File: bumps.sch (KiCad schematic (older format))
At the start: 134 parts, among them M1 CONN_1, M2 CONN_1, M3 CONN_1, P1 DIL6, P10 Mot-A, P11 Mot-A, P12 Mot-X, P13 T1, P14 T2, P15 T3, P16 MPower, P17 PWM-2, P18 PWM-1, P19 END-X, P2 DIL6, P20 END-Y, P21 END-Z, P22 Mot-X, P23 Mot-Y, P24 Mot-Y, P25 Mot-Z, P26 Mot-Z, P27 Aux, P28 KillSwitch, P29 PWM, P3 Mot-E, P4 Mot-E, P5 DIL6, P6 DIL6, P7 DIL6, P8 P8 Header, P9 P9 Header, Q1 IRLB8743PBF, Q2 IRLB8743PBF, Q3 FDS9926A, Q4 FDS9926A, U1 Motor-2, U2 Motor-4, U3 Motor-5, U4 Motor-3, U5 Motor-1, U6 MC34063, U7 AP1117/3.3, U8 Opto

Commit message: o Adding fuse holder (footprint and schematic). o .. work in progress. Attempt to make things fit.
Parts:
- removed F1: FUSE, Fuse_Holders_and_Fuses:Fuse_TE5_Littlefuse-395Series, symbol FUSE
- added P30, P31: CONN_01X01, bumps:FuseBlade, symbol CONN_01X01
- R2, R3: footprint SMD_Packages:SM0805 -> Resistors_SMD:R_0805
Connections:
- net labels added: Power-IN
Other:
- moved on the sheet: M1, M2, M3
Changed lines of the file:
@@
-	1    0    0    -1
-$EndComp
-$Comp
-L FUSE F1
-U 1 1 52EE1508
-P 1550 9050
-F 0 "F1" H 1650 9100 40  0000 C CNN
-F 1 "FUSE" H 1450 9000 40  0000 C CNN
-F 2 "Fuse_Holders_and_Fuses:Fuse_TE5_Littlefuse-395Series" H 1550 9050 60  0001 C CNN
-F 3 "" H 1550 9050 60  0000 C CNN
-	1    1550 9050
 	1    0    0    -1
 $EndComp
@@
 L PWR_FLAG #FLG036
 U 1 1 53019B49
-P 1850 9000
-F 0 "#FLG036" H 1850 9095 30  0001 C CNN
-F 1 "PWR_FLAG" H 1850 9180 30  0000 C CNN
-F 2 "" H 1850 9000 60  0001 C CNN
-F 3 "" H 1850 9000 60  0000 C CNN
-	1    1850 9000
-	1    0    0    -1
+P 1850 9100
+F 0 "#FLG036" H 1850 9195 30  0001 C CNN
+F 1 "PWR_FLAG" H 1850 9280 30  0000 C CNN
+F 2 "" H 1850 9100 60  0001 C CNN
+F 3 "" H 1850 9100 60  0000 C CNN
+	1    1850 9100
+	-1   0    0    1
 $EndComp
 $Comp
@@
 L CONN_01X01 M1
 U 1 1 53137A56
-P 1800 9450
-F 0 "M1" H 1880 9450 40  0000 L CNN
-F 1 "CONN_1" H 1800 9505 30  0001 C CNN
-F 2 "Connect:1pin" H 1800 9450 60  0001 C CNN
-F 3 "" H 1800 9450 60  0000 C CNN
-	1    1800 9450
+P 2750 9500
+F 0 "M1" H 2830 9500 40  0000 L CNN
+F 1 "CONN_1" H 2750 9555 30  0001 C CNN
+F 2 "Connect:1pin" H 2750 9500 60  0001 C CNN
+F 3 "" H 2750 9500 60  0000 C CNN
+	1    2750 9500
 	0    -1   -1   0
 $EndComp
@@
 L CONN_01X01 M2
 U 1 1 53137A6A
-P 2000 9450
-F 0 "M2" H 2080 9450 40  0000 L CNN
-F 1 "CONN_1" H 2000 9505 30  0001 C CNN
-F 2 "Connect:1pin" H 2000 9450 60  0001 C CNN
-F 3 "" H 2000 9450 60  0000 C CNN
-	1    2000 9450
+P 2950 9500
+F 0 "M2" H 3030 9500 40  0000 L CNN
+F 1 "CONN_1" H 2950 9555 30  0001 C CNN
+F 2 "Connect:1pin" H 2950 9500 60  0001 C CNN
+F 3 "" H 2950 9500 60  0000 C CNN
+	1    2950 9500
 	0    -1   -1   0
 $EndComp
@@
 L CONN_01X01 M3
 U 1 1 5313908A
-P 2200 9450
-F 0 "M3" H 2280 9450 40  0000 L CNN
-F 1 "CONN_1" H 2200 9505 30  0001 C CNN
-F 2 "Connect:1pin" H 2200 9450 60  0001 C CNN
-F 3 "" H 2200 9450 60  0000 C CNN
-	1    2200 9450
+P 3150 9500
+F 0 "M3" H 3230 9500 40  0000 L CNN
+F 1 "CONN_1" H 3150 9555 30  0001 C CNN
+F 2 "Connect:1pin" H 3150 9500 60  0001 C CNN
+F 3 "" H 3150 9500 60  0000 C CNN
+	1    3150 9500
 	0    -1   -1   0
 $EndComp
@@
 F 0 "R3" V 10500 8150 40  0000 C CNN
 F 1 "4k7" V 10607 8151 40  0000 C CNN
-F 2 "SMD_Packages:SM0805" V 10530 8150 30  0001 C CNN
+F 2 "Resistors_SMD:R_0805" V 10530 8150 30  0001 C CNN
 F 3 "" H 10600 8150 30  0000 C CNN
 	1    10600 8150
@@
 F 0 "R2" V 8550 7850 40  0000 C CNN
 F 1 "330" V 8657 7851 40  0000 C CNN
-F 2 "SMD_Packages:SM0805" V 8580 7850 30  0001 C CNN
+F 2 "Resistors_SMD:R_0805" V 8580 7850 30  0001 C CNN
 F 3 "" H 8650 7850 30  0000 C CNN
 	1    8650 7850
@@
 	1150 9050 1300 9050
 Wire Wire Line
-	1800 9050 2000 9050
+	1650 9050 2000 9050
 Wire Wire Line
 	4300 8500 4650 8500
@@
 Connection ~ 3450 7950
 Connection ~ 3450 7700
-Wire Wire Line
-	1850 9000 1850 9050
 Connection ~ 1850 9050
 Wire Wire Line
@@
 	-1   0    0    1
 $EndComp
+$Comp
+L CONN_01X01 P30
+U 1 1 5570EE85
+P 1300 8850
+F 0 "P30" H 1300 8950 50  0000 C CNN
+F 1 "CONN_01X01" V 1400 8850 50  0000 C CNN
+F 2 "bumps:FuseBlade" H 1300 8850 60  0001 C CNN
+F 3 "" H 1300 8850 60  0000 C CNN
+	1    1300 8850
+	0    -1   -1   0
+$EndComp
+Wire Wire Line
+	1850 9050 1850 9100
+$Comp
+L CONN_01X01 P31
+U 1 1 5570F5CA
+P 1650 8850
+F 0 "P31" H 1650 8950 50  0000 C CNN
+F 1 "CONN_01X01" V 1750 8850 50  0000 C CNN
+F 2 "bumps:FuseBlade" H 1650 8850 60  0001 C CNN
+F 3 "" H 1650 8850 60  0000 C CNN
+	1    1650 8850
+	0    -1   -1   0
+$EndComp
+Text Label 850  9000 0    60   ~ 0
+Power-IN
 $EndSCHEMATC

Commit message: o intermediate state.
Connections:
- wire segments 260 -> 255
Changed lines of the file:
@@
 	5800 4650 5800 4700
 Wire Wire Line
-	4300 4350 4300 4450
-Wire Wire Line
 	3900 4050 4300 4050
 Wire Wire Line
@@
 Wire Wire Line
 	9950 5050 9950 5100
-Wire Wire Line
-	8450 4750 8450 4850
 Wire Wire Line
 	7250 4250 7250 4650
@@
 	9950 1750 9950 1800
 Wire Wire Line
-	8450 1450 8450 1550
-Wire Wire Line
 	7250 950  7250 1350
 Connection ~ 7250 1150
@@
 	9950 3400 9950 3450
 Wire Wire Line
-	8450 3100 8450 3200
-Wire Wire Line
 	7250 2600 7250 3000
 Connection ~ 7250 2800
@@
 Wire Wire Line
 	5800 6400 5800 6450
-Wire Wire Line
-	4300 6100 4300 6200
 Wire Wire Line
 	3100 5600 3100 6000
@@
 Text Label 850  9000 0    60   ~ 0
 Power-IN
+Text GLabel 4300 4350 0    60   Input ~ 0
+~EStop
+Text GLabel 4300 6100 0    60   Input ~ 0
+~EStop
+Text GLabel 8450 4750 0    60   Input ~ 0
+~EStop
+Text GLabel 8450 3100 0    60   Input ~ 0
+~EStop
+Text GLabel 8450 1450 0    60   Input ~ 0
+~EStop
 $EndSCHEMATC

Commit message: o Bring to latest state of kicad library. o Now checking in also bumps-cache: learned that it   is effectively the 'project library' keeping track of   the symbols being used. o (was done in a branch, squashed together now).
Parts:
- C1, C12, C2, C3, C4, C5, C7, C8: symbol CAPAPOL -> CP
- D1: symbol DIODESCH -> D_Schottky
- D10, D11: footprint Diodes_ThroughHole:Diode_DO-41_SOD81_Vertical_KathodeUp -> Diodes_ThroughHole:Diode_DO-41_SOD81_Vertical_AnodeUp; symbol DIODE -> D_Schottky
- D12, D13, D14, D15, D16, D17, D18, D19, D20, D21: symbol LED -> Led_Small
- Q1, Q2: footprint Transistors_TO-220:TO-220_FET-GDS_Vertical_LargePads -> Transistors_TO-220:TO-220_Neutral123_Vertical_LargePads; symbol MOSFET_N -> Q_NMOS_GDS
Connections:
- wire segments 255 -> 252
- no-connect marks 47 -> 52
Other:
- moved on the sheet: C13, C14, C15, C16, C17, C20, C21, C22, C23, C24, C6, D2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

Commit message: o use standard opto PC817 footprint.
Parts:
- U8: value Opto -> PC817; symbol OPTO-TRANSISTOR4 -> PC817
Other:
- moved on the sheet: P28, R2, R3
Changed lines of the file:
@@
 VDD_3V3
 $Comp
-L OPTO-TRANSISTOR4 U8
+L PC817 U8
 U 1 1 556F9659
-P 9550 8000
-F 0 "U8" H 9750 8250 60  0000 C CNN
-F 1 "Opto" H 9550 7750 60  0000 C CNN
-F 2 "bumps:DIL-4" H 9550 8000 60  0001 C CNN
-F 3 "" H 9550 8000 60  0000 C CNN
-	1    9550 8000
+P 8350 7900
+F 0 "U8" H 8200 7650 60  0000 C CNN
+F 1 "PC817" H 8450 7650 60  0000 C CNN
+F 2 "bumps:DIL-4" H 8350 7900 60  0001 C CNN
+F 3 "" H 8350 7900 60  0000 C CNN
+	1    8350 7900
 	1    0    0    -1
 $EndComp
@@
 L R R3
 U 1 1 556FE6AB
-P 10500 8150
-F 0 "R3" V 10600 8150 40  0000 C CNN
-F 1 "4k7" V 10507 8151 40  0000 C CNN
-F 2 "Resistors_SMD:R_0805" V 10430 8150 30  0001 C CNN
-F 3 "" H 10500 8150 30  0000 C CNN
-	1    10500 8150
+P 8800 8000
+F 0 "R3" V 8900 8000 40  0000 C CNN
+F 1 "4k7" V 8807 8001 40  0000 C CNN
+F 2 "Resistors_SMD:R_0805" V 8730 8000 30  0001 C CNN
+F 3 "" H 8800 8000 30  0000 C CNN
+	1    8800 8000
 	0    -1   1    0
 $EndComp
-Text GLabel 10150 7850 2    50   Input ~ 0
+Text GLabel 8650 7800 2    50   Input ~ 0
 VDD_3V3
-Text GLabel 10250 8000 2    60   Output ~ 0
+Text GLabel 9050 7900 2    60   Output ~ 0
 ~EStop
 $Comp
 L GND #PWR051
 U 1 1 55714D22
-P 10650 8200
-F 0 "#PWR051" H 10650 8200 30  0001 C CNN
-F 1 "GND" H 10650 8130 30  0001 C CNN
-F 2 "" H 10650 8200 60  0001 C CNN
-F 3 "" H 10650 8200 60  0000 C CNN
-	1    10650 8200
+P 8950 8050
+F 0 "#PWR051" H 8950 8050 30  0001 C CNN
+F 1 "GND" H 8950 7980 30  0001 C CNN
+F 2 "" H 8950 8050 60  0001 C CNN
+F 3 "" H 8950 8050 60  0000 C CNN
+	1    8950 8050
 	-1   0    0    -1
 $EndComp
-Text Notes 8800 7750 0    60   ~ 0
+Text Notes 7550 7700 0    60   ~ 0
 Normal case: LED on, ~EStop~ pulled to High.
 $Comp
 L R R2
 U 1 1 557180A7
-P 8750 7850
-F 0 "R2" V 8650 7850 40  0000 C CNN
-F 1 "330" V 8757 7851 40  0000 C CNN
-F 2 "Resistors_SMD:R_0805" V 8680 7850 30  0001 C CNN
-F 3 "" H 8750 7850 30  0000 C CNN
-	1    8750 7850
+P 7900 7800
+F 0 "R2" V 7800 7800 40  0000 C CNN
+F 1 "330" V 7907 7801 40  0000 C CNN
+F 2 "Resistors_SMD:R_0805" V 7830 7800 30  0001 C CNN
+F 3 "" H 7900 7800 30  0000 C CNN
+	1    7900 7800
 	0    -1   1    0
 $EndComp
-Text GLabel 8600 7850 0    50   Input ~ 0
+Text GLabel 7750 7800 0    50   Input ~ 0
 VDD_5V
 $Comp
 L GND #PWR052
 U 1 1 5571A73C
-P 8500 8250
-F 0 "#PWR052" H 8500 8250 30  0001 C CNN
-F 1 "GND" H 8500 8180 30  0001 C CNN
-F 2 "" H 8500 8250 60  0001 C CNN
-F 3 "" H 8500 8250 60  0001 C CNN
-	1    8500 8250
+P 7650 8150
+F 0 "#PWR052" H 7650 8150 30  0001 C CNN
+F 1 "GND" H 7650 8080 30  0001 C CNN
+F 2 "" H 7650 8150 60  0001 C CNN
+F 3 "" H 7650 8150 60  0001 C CNN
+	1    7650 8150
 	1    0    0    -1
 $EndComp
-Text Notes 7850 8000 0    60   ~ 0
+Text Notes 7300 8250 1    60   ~ 0
 Switch NC
 Wire Wire Line
@@
 Connection ~ 4500 1250
 Wire Wire Line
-	10150 8150 10350 8150
-Wire Wire Line
-	10250 8000 10200 8000
-Wire Wire Line
-	10200 8000 10200 8150
-Connection ~ 10200 8150
-Wire Wire Line
-	10650 8150 10650 8200
-Wire Wire Line
-	8500 8100 8900 8100
-Wire Wire Line
-	8900 8100 8900 8150
-Wire Wire Line
-	8500 8200 8500 8200
-Wire Wire Line
-	8500 8200 8500 8250
+	8950 8000 8950 8050
+Wire Wire Line
+	7650 8000 8050 8000
+Wire Wire Line
+	7650 8100 7650 8100
+Wire Wire Line
+	7650 8100 7650 8150
 $Comp
 L CONN_01X02 P28
 U 1 1 557008FF
-P 8300 8150
-F 0 "P28" H 8300 8300 50  0000 C CNN
-F 1 "KillSwitch" V 8400 8150 50  0000 C CNN
-F 2 "bumps:WideHeader" H 8300 8150 60  0001 C CNN
-F 3 "" H 8300 8150 60  0000 C CNN
-	1    8300 8150
+P 7450 8050
+F 0 "P28" H 7450 8200 50  0000 C CNN
+F 1 "KillSwitch" V 7550 8050 50  0000 C CNN
+F 2 "bumps:WideHeader" H 7450 8050 60  0001 C CNN
+F 3 "" H 7450 8050 60  0000 C CNN
+	1    7450 8050
 	-1   0    0    1
 $EndComp
@@
 Wire Wire Line
 	2000 7150 2050 7150
+Wire Wire Line
+	8650 8000 8650 7900
+Wire Wire Line
+	8650 7900 9050 7900
 $EndSCHEMATC

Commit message: o Use some current standard components.
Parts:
- C13, C15, C16, C17, C20, C21, C22, C23, C24, C6: footprint SMD_Packages:SM0805 -> Capacitors_SMD:C_0805
- Q3, Q4, U6: footprint SOIC_Packages:SOIC-8_N -> Housings_SOIC:SOIC-8_3.9x4.9mm_Pitch1.27mm
- R10, R11, R12, R13, R14, R15, R16, R17, R18, R19, R20, R21, R22, R23, R24, R25, R26, R27, R28, R29, R30, R31, R32, R33, R34, R35, R36, R37, R38, R39, R40, R41, R42, R43, R6, R7, R8, R9: footprint SMD_Packages:SM0805 -> Resistors_SMD:R_0805
- U8: footprint bumps:DIL-4 -> Housings_DIP:DIP-4_W7.62mm

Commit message: o More standard footprint conversions.
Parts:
- D5, D6, D7: footprint SMD_Packages:SOT23 -> Housings_SOT-23_SOT-143_TSOT-6:SOT-23
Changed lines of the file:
@@
 F 0 "D7" V 10700 6200 60  0000 L CNN
 F 1 "BAT54S" V 10700 5800 60  0000 L CNN
-F 2 "SMD_Packages:SOT23" H 10600 6050 60  0001 C CNN
+F 2 "Housings_SOT-23_SOT-143_TSOT-6:SOT-23" H 10600 6050 60  0001 C CNN
 F 3 "" H 10600 6050 60  0000 C CNN
 	1    10600 6050
@@
 F 0 "D6" V 9500 6150 60  0000 L CNN
 F 1 "BAT54S" V 9500 5800 60  0000 L CNN
-F 2 "SMD_Packages:SOT23" H 9400 6050 60  0001 C CNN
+F 2 "Housings_SOT-23_SOT-143_TSOT-6:SOT-23" H 9400 6050 60  0001 C CNN
 F 3 "" H 9400 6050 60  0000 C CNN
 	1    9400 6050
@@
 F 0 "D5" V 8300 6200 60  0000 L CNN
 F 1 "BAT54S" V 8300 5800 60  0000 L CNN
-F 2 "SMD_Packages:SOT23" H 8200 6050 60  0001 C CNN
+F 2 "Housings_SOT-23_SOT-143_TSOT-6:SOT-23" H 8200 6050 60  0001 C CNN
 F 3 "" H 8200 6050 60  0000 C CNN
 	1    8200 6050

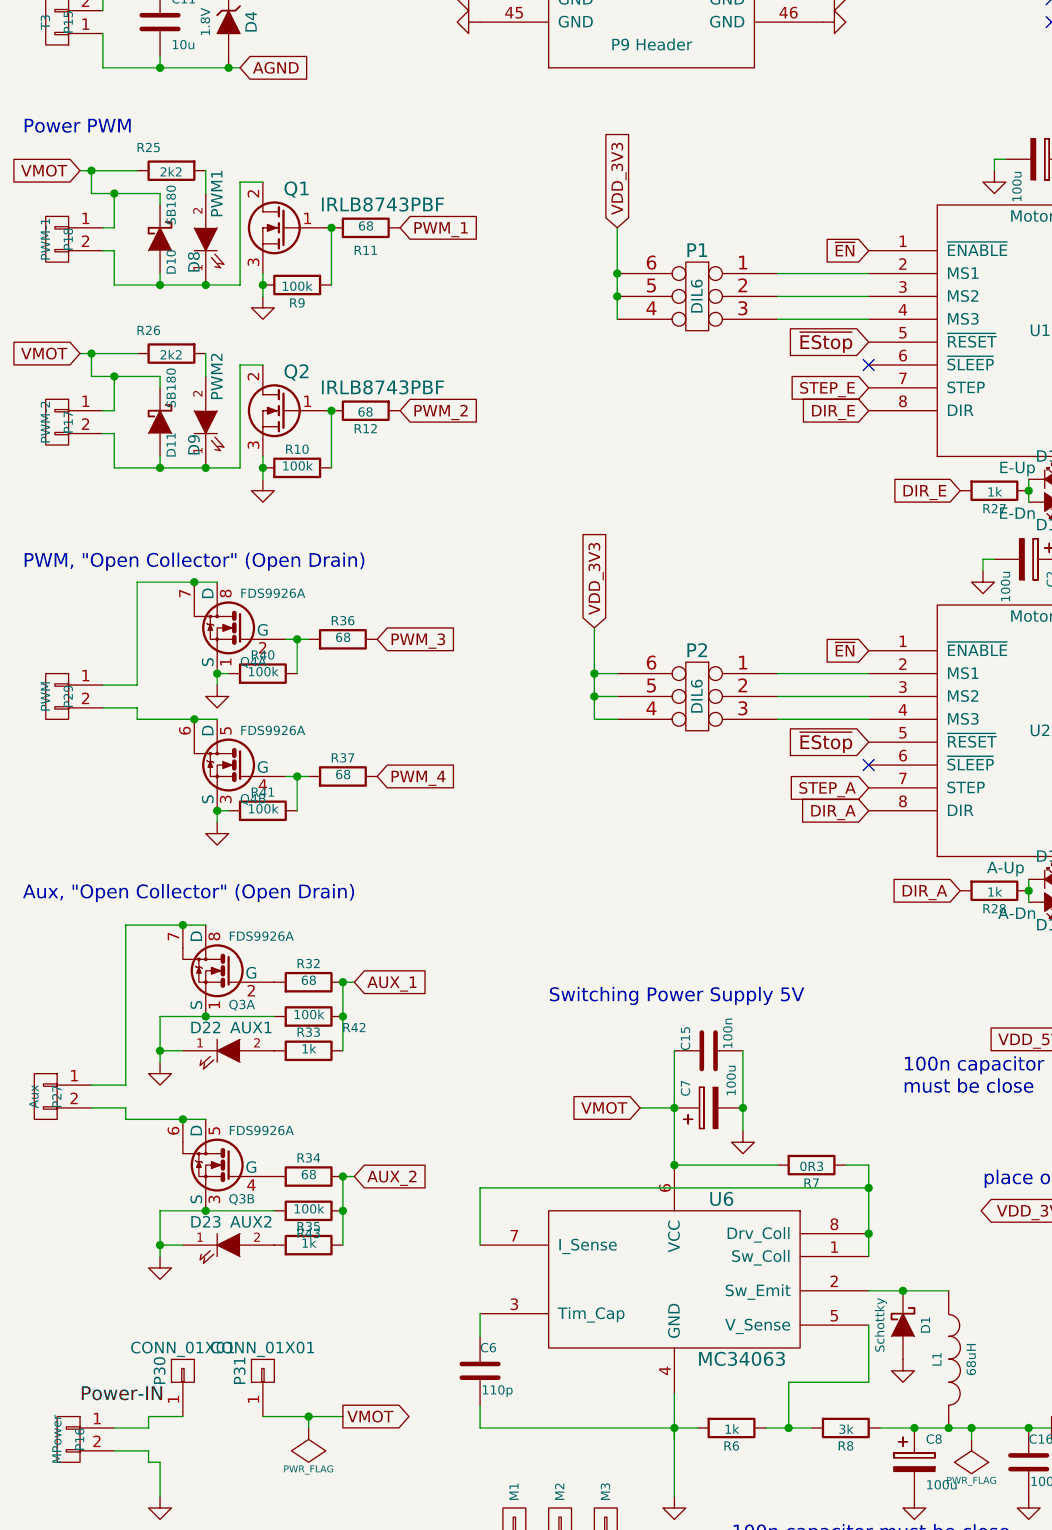
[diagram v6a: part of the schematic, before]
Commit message: o Design for Manufacturing: choose the same kind of diode for the   switching power supply and the snubber diode to reduce different   component BOM count.
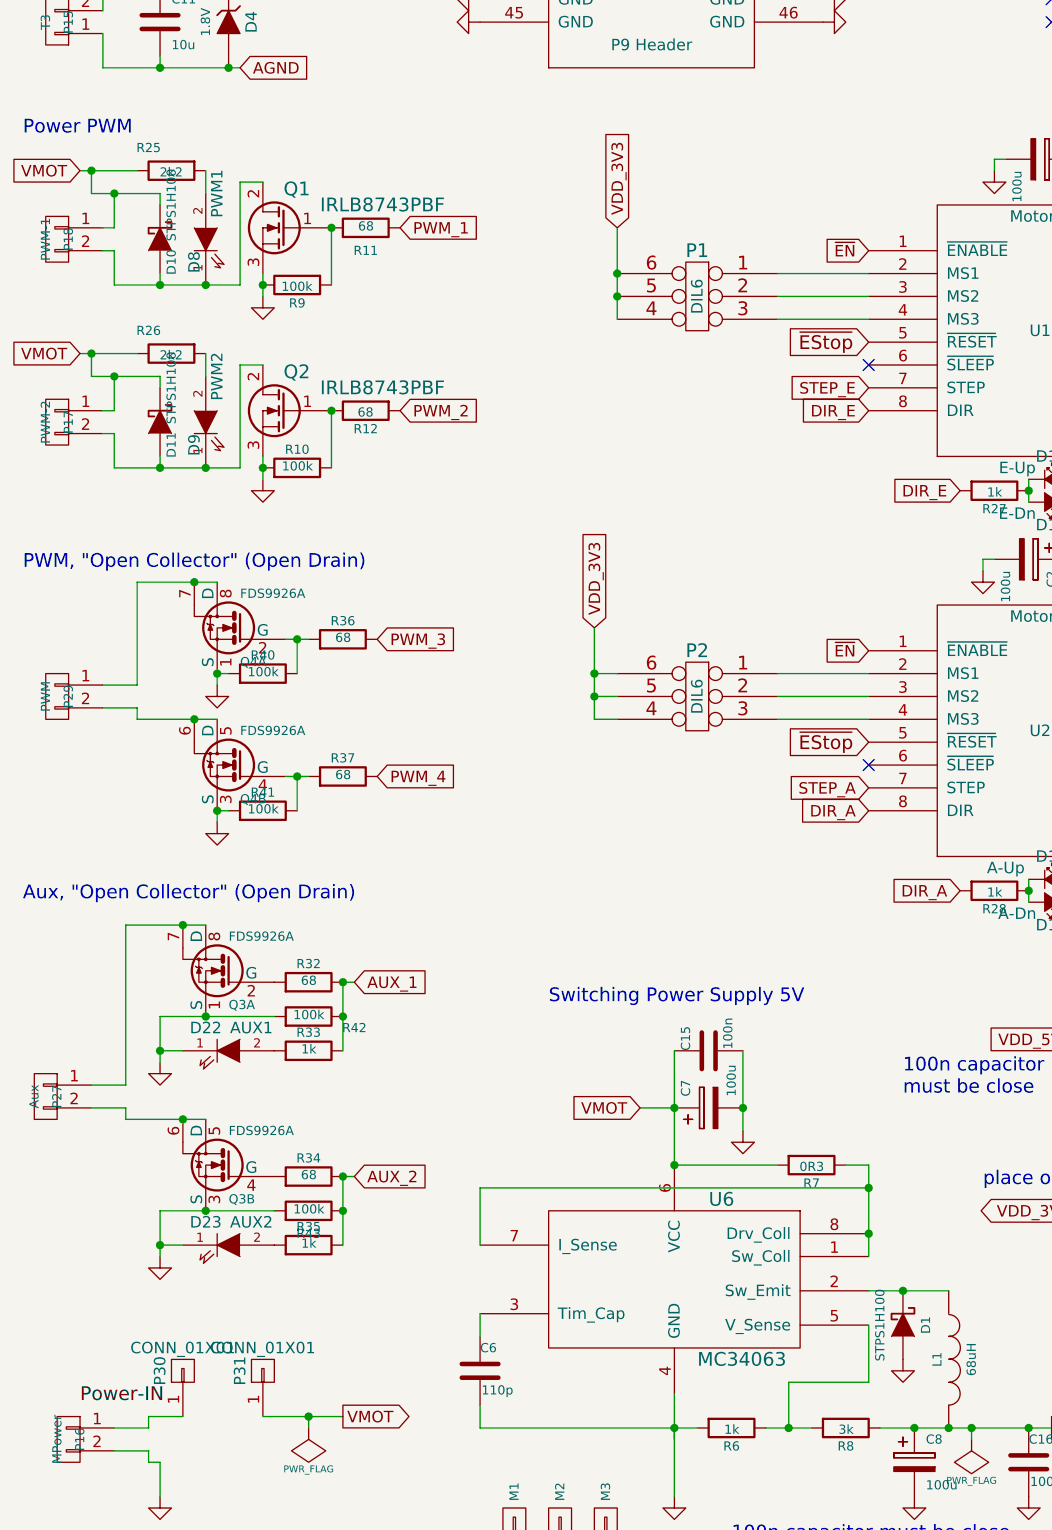
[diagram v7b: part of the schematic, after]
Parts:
- D1: value Schottky -> STPS1H100; footprint Diodes_SMD:Diode-MiniMELF_Standard -> Diodes_SMD:Diode-SMB_Standard
- D10, D11: value SB180 -> STPS1H100; footprint Diodes_ThroughHole:Diode_DO-41_SOD81_Vertical_AnodeUp -> Diodes_SMD:Diode-SMB_Standard
- D2, D3, D4: footprint Diodes_SMD:Diode-MiniMELF_Standard -> Diodes_SMD:SOD-123
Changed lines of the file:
@@
 P 4450 8650
 F 0 "D1" H 4450 8750 40  0000 C CNN
-F 1 "Schottky" H 4450 8550 40  0000 C CNN
-F 2 "Diodes_SMD:Diode-MiniMELF_Standard" H 4450 8650 60  0001 C CNN
-F 3 "" H 4450 8650 60  0000 C CNN
+F 1 "STPS1H100" H 4450 8550 40  0000 C CNN
+F 2 "Diodes_SMD:Diode-SMB_Standard" H 4450 8650 60  0001 C CNN
+F 3 "http://www.st.com/web/en/resource/technical/document/datasheet/CD00001304.pdf" H 4450 8650 60  0001 C CNN
 	1    4450 8650
 	0    1    1    0
@@
 F 0 "D3" H 1500 2150 50  0000 C CNN
 F 1 "1.8V" H 1500 1950 40  0000 C CNN
-F 2 "Diodes_SMD:Diode-MiniMELF_Standard" H 1500 2050 60  0001 C CNN
+F 2 "Diodes_SMD:SOD-123" H 1500 2050 60  0001 C CNN
 F 3 "" H 1500 2050 60  0000 C CNN
 	1    1500 2050
@@
 F 0 "D2" H 1500 1250 50  0000 C CNN
 F 1 "1.8V" H 1500 1050 40  0000 C CNN
-F 2 "Diodes_SMD:Diode-MiniMELF_Standard" H 1500 1150 60  0001 C CNN
+F 2 "Diodes_SMD:SOD-123" H 1500 1150 60  0001 C CNN
 F 3 "" H 1500 1150 60  0000 C CNN
 	1    1500 1150
@@
 F 0 "D4" H 1500 3050 50  0000 C CNN
 F 1 "1.8V" H 1500 2850 40  0000 C CNN
-F 2 "Diodes_SMD:Diode-MiniMELF_Standard" H 1500 2950 60  0001 C CNN
+F 2 "Diodes_SMD:SOD-123" H 1500 2950 60  0001 C CNN
 F 3 "" H 1500 2950 60  0000 C CNN
 	1    1500 2950
@@
 P 1200 3900
 F 0 "D10" H 1300 3950 40  0000 C CNN
-F 1 "SB180" H 1050 3950 40  0000 C CNN
-F 2 "Diodes_ThroughHole:Diode_DO-41_SOD81_Vertical_AnodeUp" H 1200 3900 60  0001 C CNN
+F 1 "STPS1H100" H 1050 3950 40  0000 C CNN
+F 2 "Diodes_SMD:Diode-SMB_Standard" H 1200 3900 60  0001 C CNN
 F 3 "" H 1200 3900 60  0000 C CNN
 	1    1200 3900
@@
 P 1200 4700
 F 0 "D11" H 1300 4750 40  0000 C CNN
-F 1 "SB180" H 1050 4750 40  0000 C CNN
-F 2 "Diodes_ThroughHole:Diode_DO-41_SOD81_Vertical_AnodeUp" H 1200 4700 60  0001 C CNN
+F 1 "STPS1H100" H 1050 4750 40  0000 C CNN
+F 2 "Diodes_SMD:Diode-SMB_Standard" H 1200 4700 60  0001 C CNN
 F 3 "" H 1200 4700 60  0000 C CNN
 	1    1200 4700
@@
 F 1 "CONN_01X01" V 1400 8850 50  0000 C CNN
 F 2 "bumps:FuseBlade" H 1300 8850 60  0001 C CNN
-F 3 "" H 1300 8850 60  0000 C CNN
+F 3 "http://www.keyelco.com/userAssets/file/M60-2p41.pdf" H 1300 8850 60  0001 C CNN
 	1    1300 8850
 	0    -1   -1   0
@@
 F 1 "CONN_01X01" V 1750 8850 50  0000 C CNN
 F 2 "bumps:FuseBlade" H 1650 8850 60  0001 C CNN
-F 3 "" H 1650 8850 60  0000 C CNN
+F 3 "http://www.keyelco.com/userAssets/file/M60-2p41.pdf" H 1650 8850 60  0001 C CNN
 	1    1650 8850
 	0    -1   -1   0

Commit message: o Use BUK9Y43 as power PWM transistor. SMD is easier to solder.
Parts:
- removed D10, D11: STPS1H100, Diodes_SMD:Diode-SMB_Standard, symbol D_Schottky
- removed Q1: IRLB8743PBF, Transistors_TO-220:TO-220_Neutral123_Vertical_LargePads, symbol Q_NMOS_GDS
- added Q1: BUK9Y43, Power_Packages_SMD:SOT-669_LFPAK_ThermalVias-1, symbol BUK9Y43
- D1: value STPS1H100 -> STPS130A; footprint Diodes_SMD:Diode-SMB_Standard -> Diodes_SMD:Diode-SMA_Standard
- D8, D9: symbol LED -> Led_Small
- Q2: value IRLB8743PBF -> BUK9Y43; footprint Transistors_TO-220:TO-220_Neutral123_Vertical_LargePads -> Power_Packages_SMD:SOT-669_LFPAK_ThermalVias-1; symbol Q_NMOS_GDS -> BUK9Y43
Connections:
- net GND: now also Q2.1 (S), Q2.2, R10.1, Q1.1 (S), Q1.2, Q1.3; no longer R10.2
- net PWM_1: now also R11.2; no longer R11.1
- net PWM_2: now also R12.1; no longer R12.2
- net at D9.1 (K), P17.2 (P2): now also Q2.5 (D); no longer Q2.2 (D)
- net at R9.2: now also R11.1, Q1.4 (G); no longer R11.2
- net at D8.1 (K), P18.2 (P2): now also Q1.5 (D)
- new net: Q2.4 (G), R10.2, R12.2
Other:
- moved on the sheet: P17, P18, R10, R11, R12, R25, R26, R9
